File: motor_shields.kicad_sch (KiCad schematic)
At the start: 58 parts, among them IC1 BTN70301EPAXUMA1, IC2 BTN70301EPAXUMA1, IC3 BTN70301EPAXUMA1, IC4 BTN70301EPAXUMA1, IC5 BTN70301EPAXUMA1, IC6 BTN70301EPAXUMA1, IC7 BTN70301EPAXUMA1, IC8 BTN70301EPAXUMA1, J4 Conn_01x06_Pin, J5 Conn_01x06_Pin, J6 Conn_01x02_Pin, J7 Conn_01x06_Pin, J8 Conn_01x06_Pin, J9 Conn_01x02_Pin

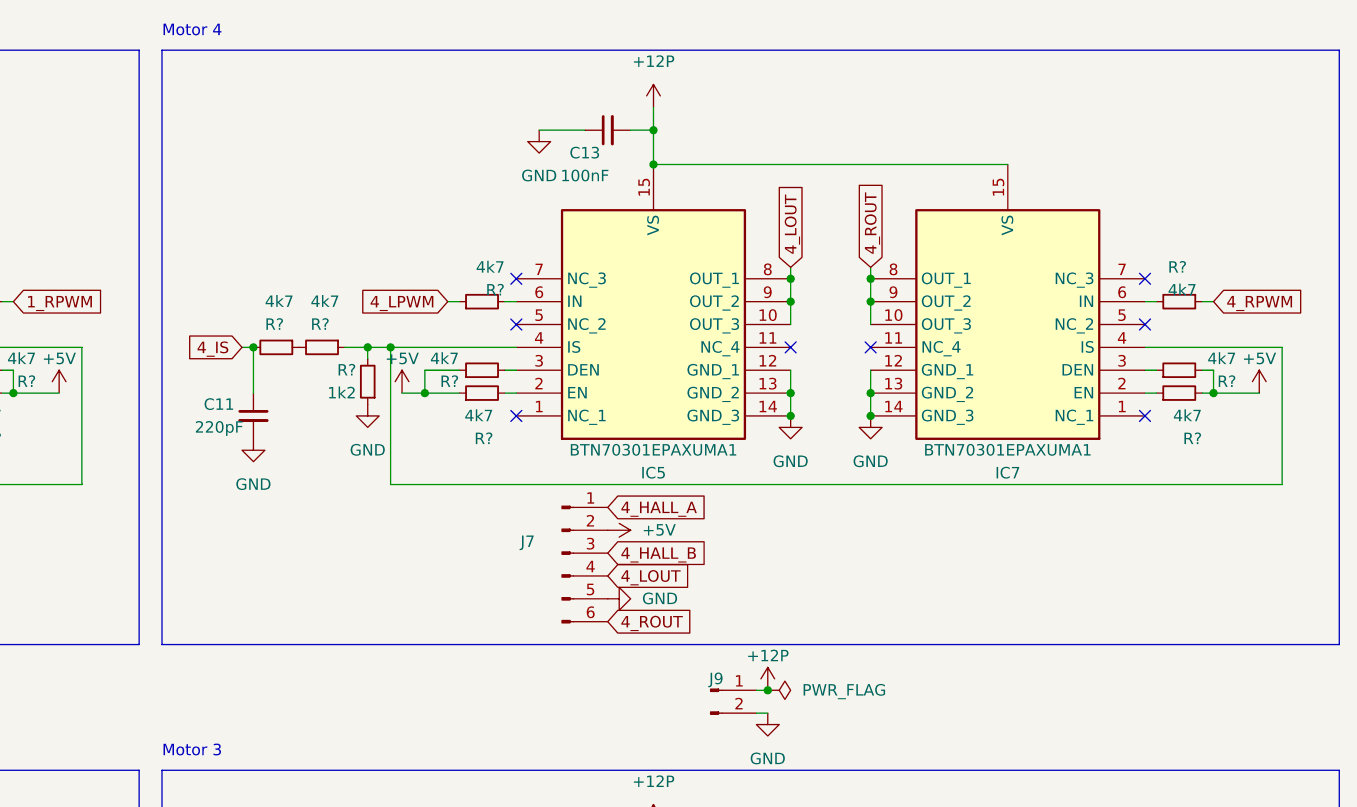
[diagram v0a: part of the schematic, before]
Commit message: 3 motor shields
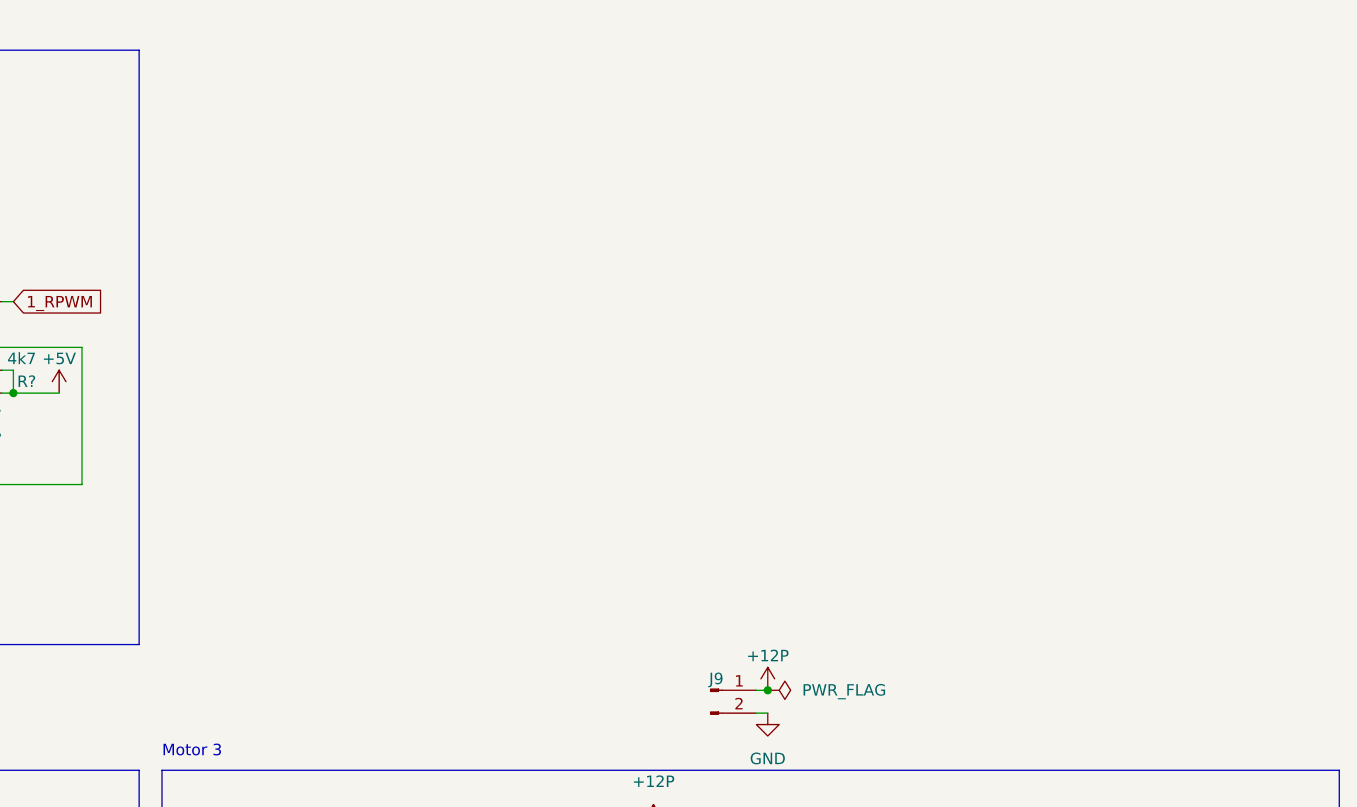
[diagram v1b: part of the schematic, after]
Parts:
- removed C11: 220pF, Capacitor_SMD:C_0402_1005Metric_Pad0.74x0.62mm_HandSolder, symbol Device:C_Small
- removed C13: 100nF, Capacitor_SMD:C_0603_1608Metric_Pad1.08x0.95mm_HandSolder, symbol Device:C_Small
- removed IC5, IC7: BTN70301EPAXUMA1, rbc Custom Library:Infineon_PG-TSDSO-14-22_custom, symbol SamacSys_Parts:BTN70301EPAXUMA1
- removed J7: Conn_01x06_Pin, Connector_Molex:Molex_Micro-Fit_3.0_43045-0612_2x03_P3.00mm_Vertical, symbol Connector:Conn_01x06_Pin
- removed R? (x8): 4k7, Resistor_SMD:R_1206_3216Metric_Pad1.30x1.75mm_HandSolder, symbol Device:R_Small
- removed R?: 1k2, Resistor_SMD:R_1206_3216Metric_Pad1.30x1.75mm_HandSolder, symbol Device:R_Small
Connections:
- no-connect marks 32 -> 24
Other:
- note removed: "Motor 4"

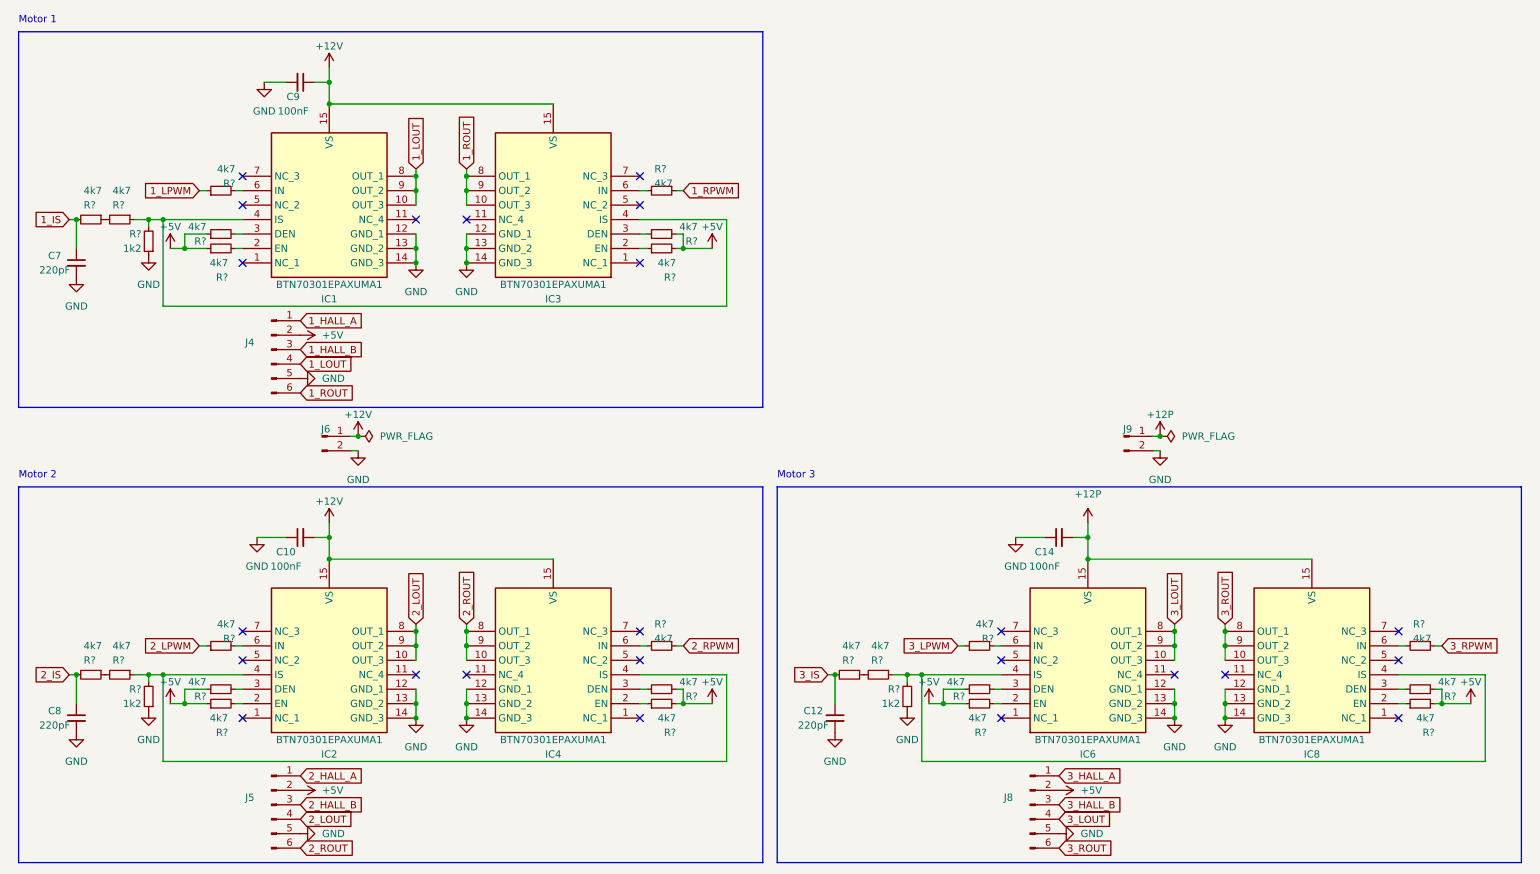
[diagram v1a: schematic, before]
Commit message: MCU migration completed
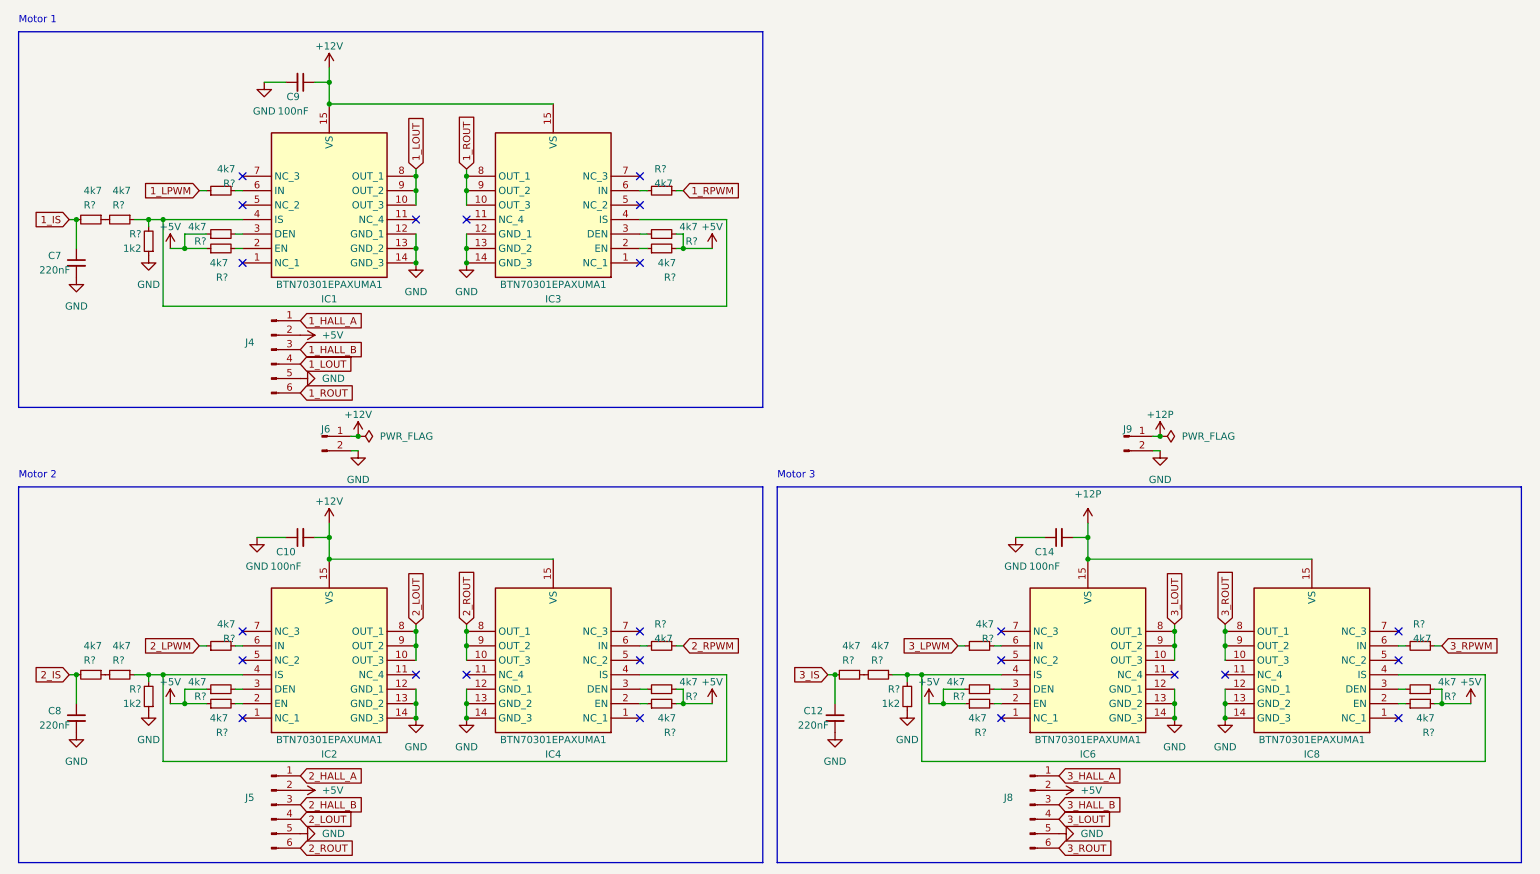
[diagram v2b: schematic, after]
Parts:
- C12, C7, C8: value 220pF -> 220nF
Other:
- title: (none) -> RBC by UGS
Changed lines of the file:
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@@
 (kicad_sch (version 20230121) (generator eeschema)
   (paper "A4")
+  (title_block
+    (title "RBC by UGS")
+    (date "2023-09-04")
+    (rev "2.0")
+  )
   (junction (at 176.53 133.35) (diameter 0) (color 0 0 0 0)
   )
@@
       (effects (font (size 1.27 1.27)))
     )
-    (property "Value" "220pF" (at 24.13 62.23 0)
+    (property "Value" "220nF" (at 24.13 62.23 0)
       (effects (font (size 1.27 1.27)))
     )
@@
       (effects (font (size 1.27 1.27)))
     )
-    (property "Value" "220pF" (at 157.48 142.24 0)
+    (property "Value" "220nF" (at 157.48 142.24 0)
       (effects (font (size 1.27 1.27)))
     )
@@
       (effects (font (size 1.27 1.27)))
     )
-    (property "Value" "220pF" (at 24.13 142.24 0)
-      (effects (font (size 1.27 1.27)))
-    )
+    (property "Value" "220nF" (at 24.13 142.24 0)
+      (effects (font (size 1.27 1.27)))
+    )

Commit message: implemented battery level detection
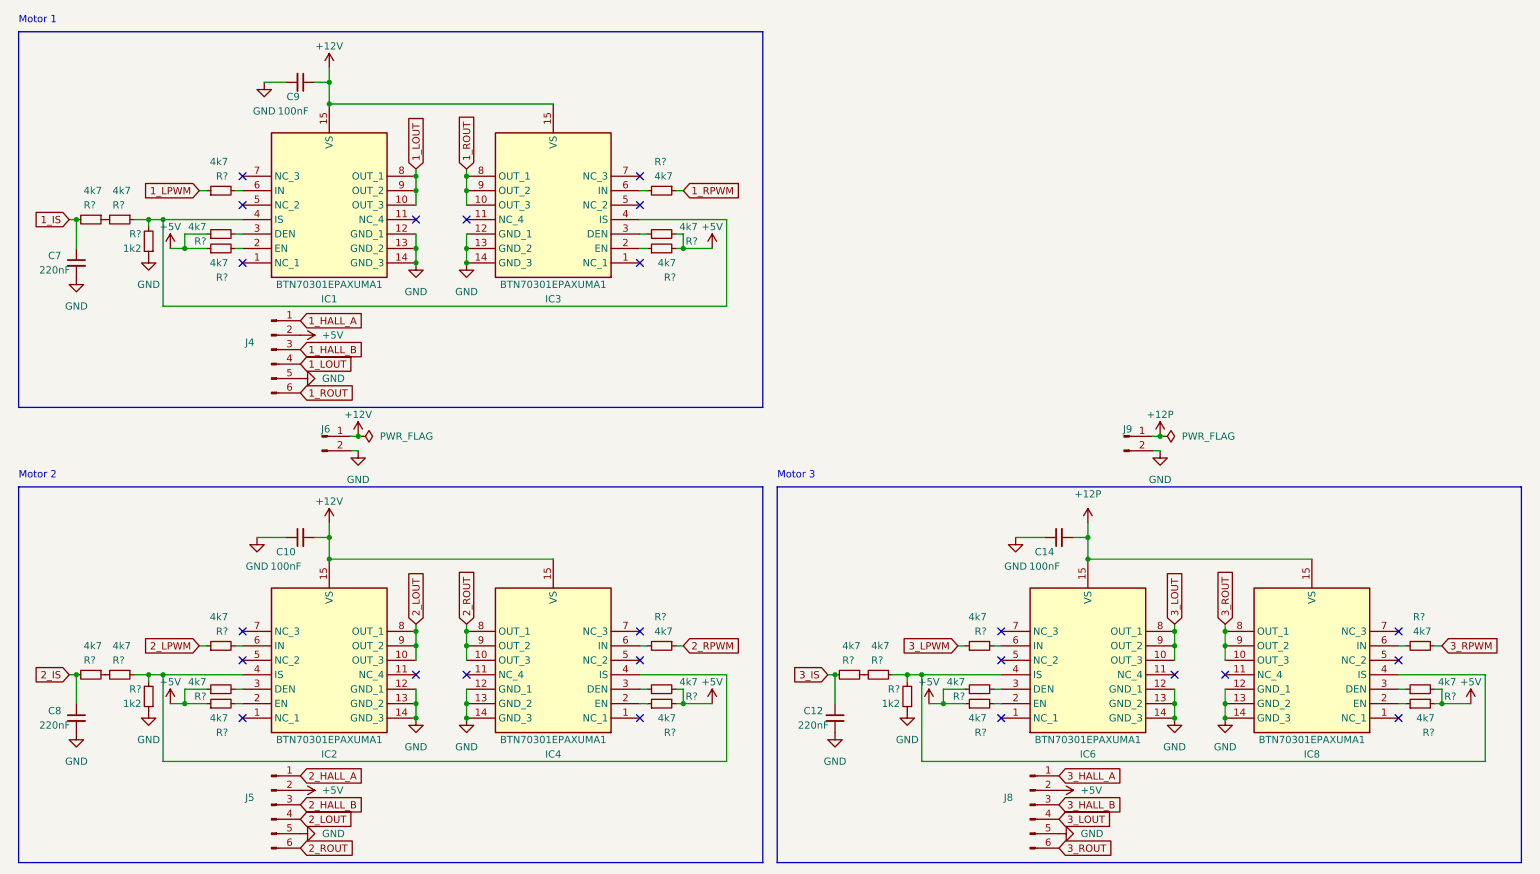
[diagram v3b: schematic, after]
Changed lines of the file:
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@@
   (symbol (lib_id "Device:R_Small") (at 130.81 128.27 270) (unit 1)
     (in_bom yes) (on_board yes) (dnp no)
-    (property "Reference" "R?" (at 129.54 124.46 90)
-      (effects (font (size 1.27 1.27)) (justify left))
-    )
-    (property "Value" "4k7" (at 129.54 127 90)
+    (property "Reference" "R?" (at 129.54 123.19 90)
+      (effects (font (size 1.27 1.27)) (justify left))
+    )
+    (property "Value" "4k7" (at 129.54 125.73 90)
       (effects (font (size 1.27 1.27)) (justify left))
     )
@@
   (symbol (lib_id "Device:R_Small") (at 264.16 128.27 270) (unit 1)
     (in_bom yes) (on_board yes) (dnp no)
-    (property "Reference" "R?" (at 262.89 124.46 90)
-      (effects (font (size 1.27 1.27)) (justify left))
-    )
-    (property "Value" "4k7" (at 262.89 127 90)
+    (property "Reference" "R?" (at 262.89 123.19 90)
+      (effects (font (size 1.27 1.27)) (justify left))
+    )
+    (property "Value" "4k7" (at 262.89 125.73 90)
       (effects (font (size 1.27 1.27)) (justify left))
     )
@@
   (symbol (lib_id "Device:R_Small") (at 130.81 48.26 270) (unit 1)
     (in_bom yes) (on_board yes) (dnp no)
-    (property "Reference" "R?" (at 129.54 44.45 90)
-      (effects (font (size 1.27 1.27)) (justify left))
-    )
-    (property "Value" "4k7" (at 129.54 46.99 90)
+    (property "Reference" "R?" (at 129.54 43.18 90)
+      (effects (font (size 1.27 1.27)) (justify left))
+    )
+    (property "Value" "4k7" (at 129.54 45.72 90)
       (effects (font (size 1.27 1.27)) (justify left))
     )
@@
   (symbol (lib_id "Device:R_Small") (at 53.34 128.27 90) (unit 1)
     (in_bom yes) (on_board yes) (dnp no)
-    (property "Reference" "R?" (at 55.88 127 90)
-      (effects (font (size 1.27 1.27)) (justify left))
-    )
-    (property "Value" "4k7" (at 55.88 124.46 90)
+    (property "Reference" "R?" (at 54.61 125.73 90)
+      (effects (font (size 1.27 1.27)) (justify left))
+    )
+    (property "Value" "4k7" (at 54.61 123.19 90)
       (effects (font (size 1.27 1.27)) (justify left))
     )
@@
   (symbol (lib_id "Device:R_Small") (at 186.69 128.27 90) (unit 1)
     (in_bom yes) (on_board yes) (dnp no)
-    (property "Reference" "R?" (at 189.23 127 90)
-      (effects (font (size 1.27 1.27)) (justify left))
-    )
-    (property "Value" "4k7" (at 189.23 124.46 90)
+    (property "Reference" "R?" (at 187.96 125.73 90)
+      (effects (font (size 1.27 1.27)) (justify left))
+    )
+    (property "Value" "4k7" (at 187.96 123.19 90)
       (effects (font (size 1.27 1.27)) (justify left))
     )
@@
   (symbol (lib_id "Device:R_Small") (at 53.34 48.26 90) (unit 1)
     (in_bom yes) (on_board yes) (dnp no)
-    (property "Reference" "R?" (at 55.88 46.99 90)
-      (effects (font (size 1.27 1.27)) (justify left))
-    )
-    (property "Value" "4k7" (at 55.88 44.45 90)
-      (effects (font (size 1.27 1.27)) (justify left))
-    )
+    (property "Reference" "R?" (at 54.61 45.72 90)
+      (effects (font (size 1.27 1.27)) (justify left))
+    )
+    (property "Value" "4k7" (at 54.61 43.18 90)
+      (effects (font (size 1.27 1.27)) (justify left))
+    )

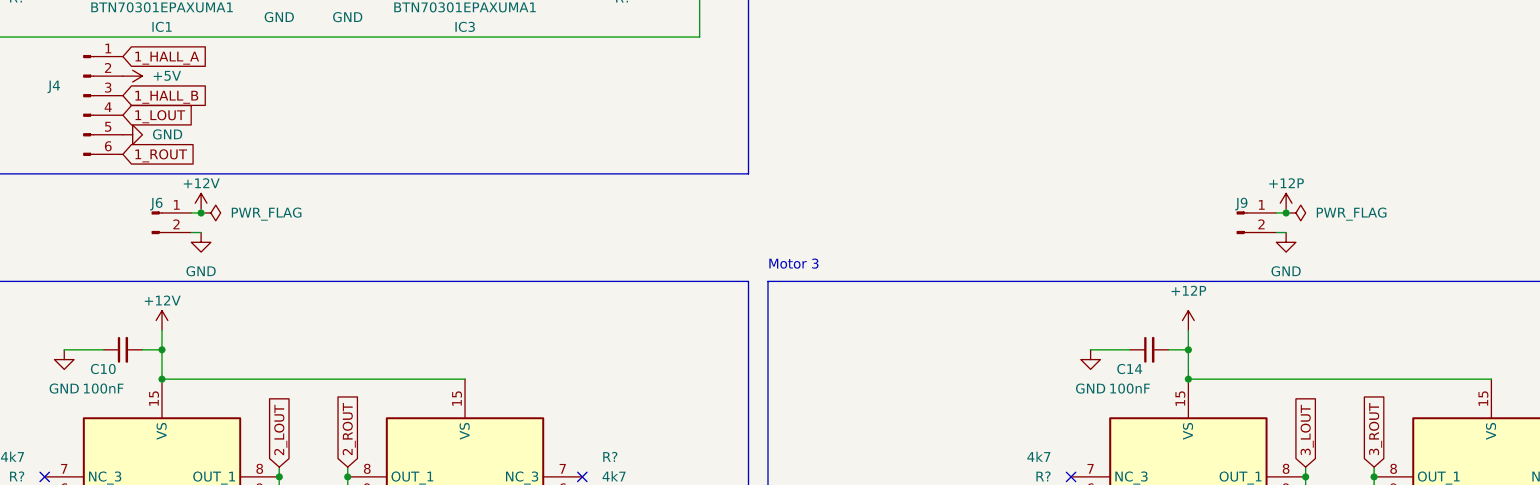
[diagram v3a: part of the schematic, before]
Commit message: completed 12V regulators
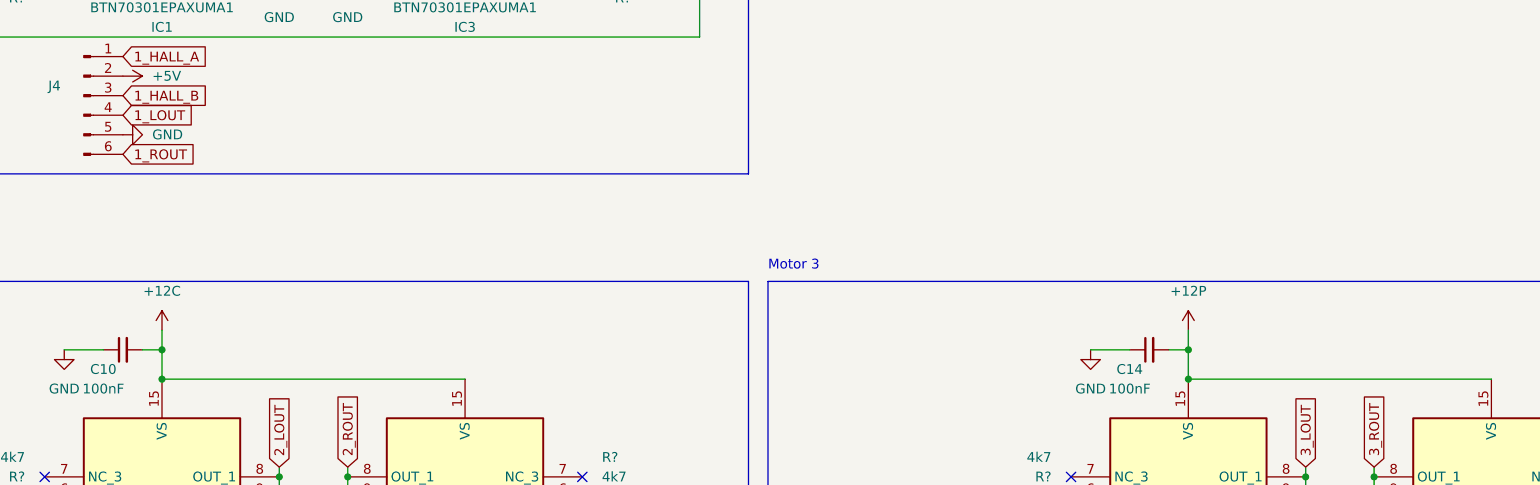
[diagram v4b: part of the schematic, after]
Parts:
- removed J6, J9: Conn_01x02_Pin, TerminalBlock_Phoenix:TerminalBlock_Phoenix_MKDS-3-2-5.08_1x02_P5.08mm_Horizontal, symbol Connector:Conn_01x02_Pin
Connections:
- net +12V: no longer C10.2, IC2.15 (VS), IC4.15 (VS)
- new net +12C: C10.2, IC2.15 (VS), IC4.15 (VS)
